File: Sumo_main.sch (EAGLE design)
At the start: 32 parts, among them U1 ATMEGA8U2AU, U2 SN65HVD3082, X1 MINI USB, X2 RS485, X4 IR Sensor 1, X5 IR Sensor 2, X6 IR Sensor 3, Y1 16MHz

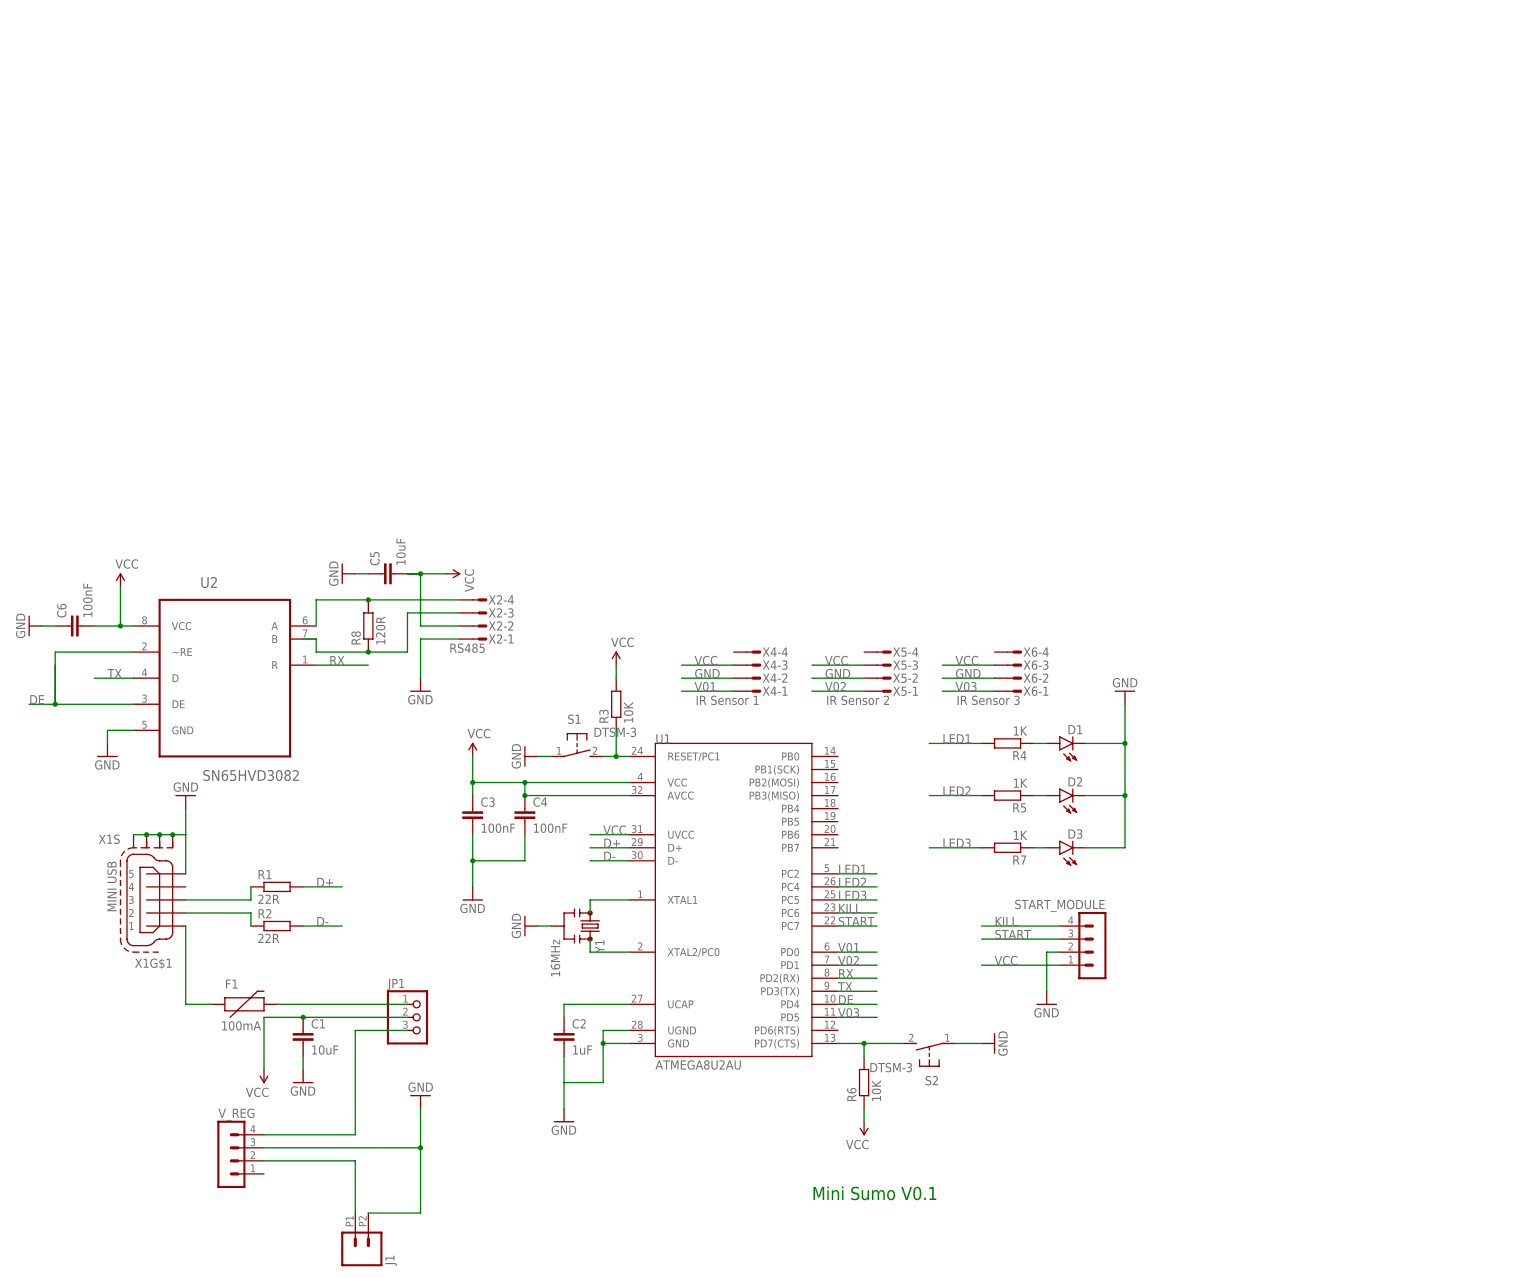
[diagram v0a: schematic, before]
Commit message: Version 2 - added comparator for sensor signals, redesigned board to be more compact.
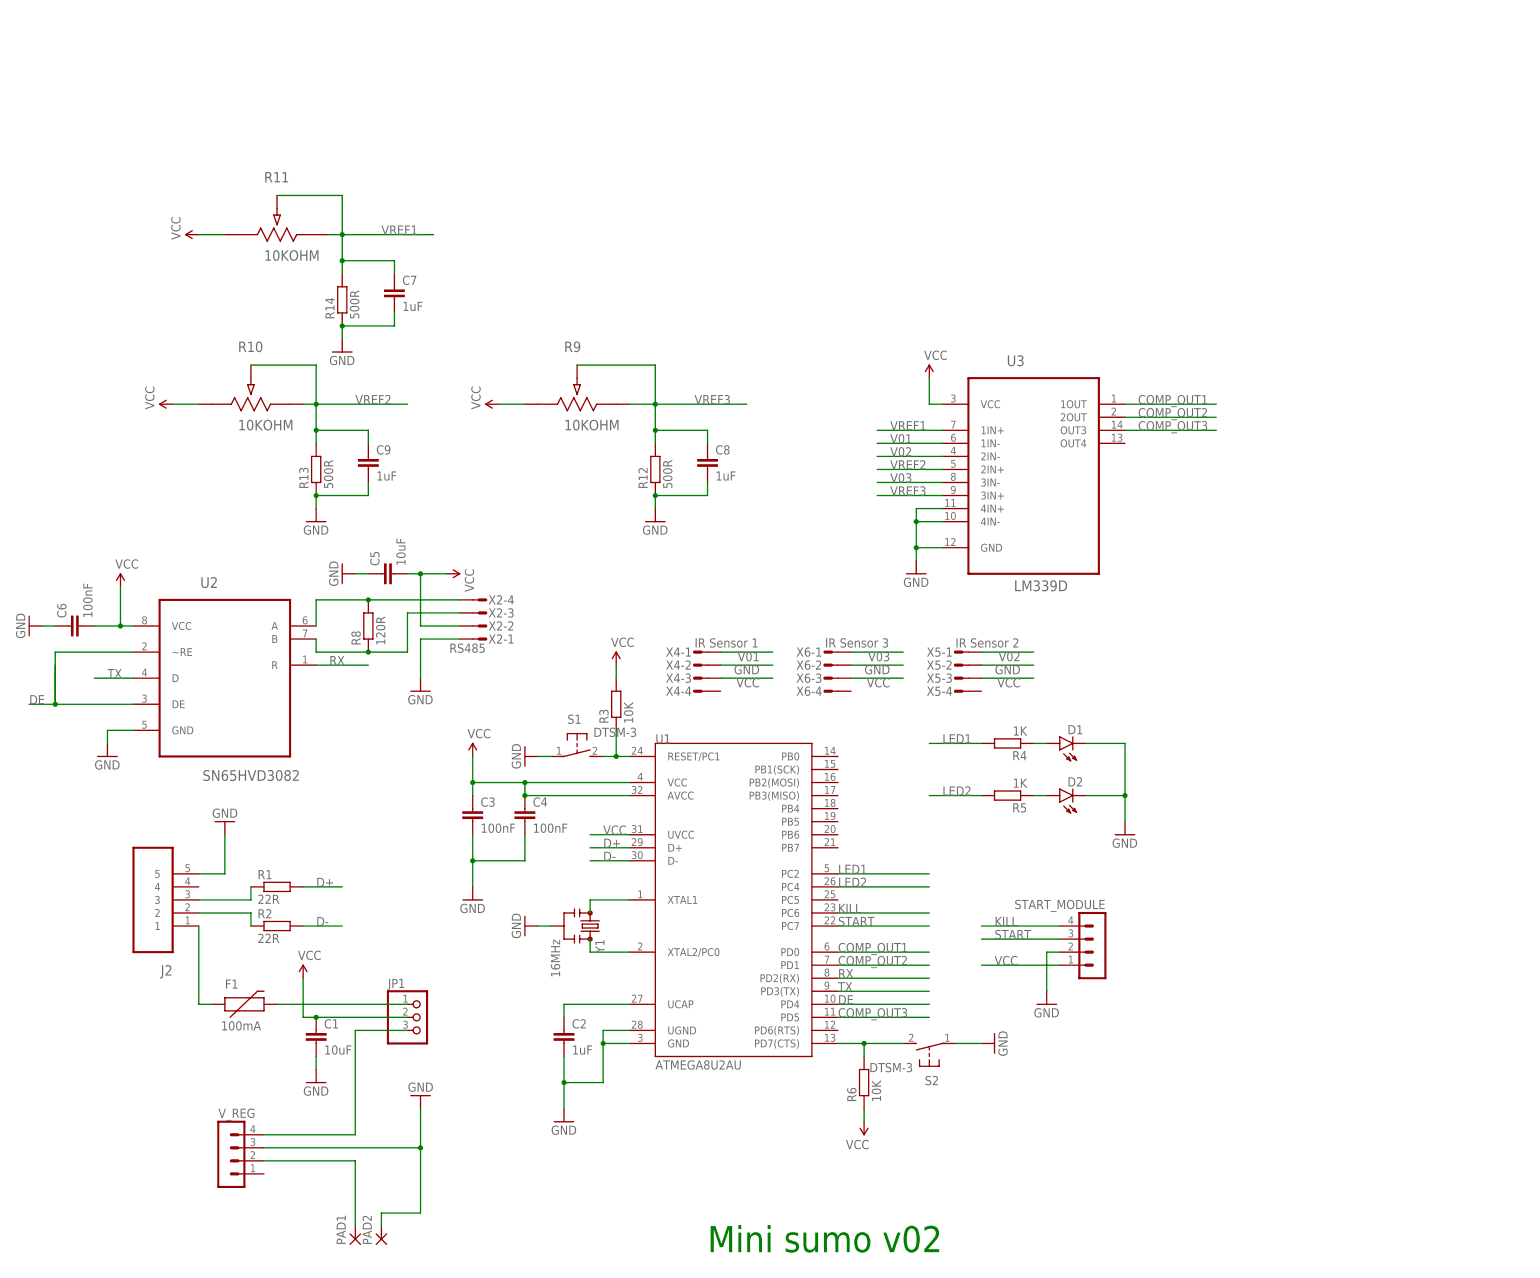
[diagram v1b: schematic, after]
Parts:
- removed D3: (no value), SparkFun-LED:LED0603
- removed J1: (no value), SparkFun-Connectors:M022.54MM_SCREWTERM
- removed R7: 1K, resistor:R-EU_R0603
- removed X1: MINI USB, con-cypressindustries:MINI-USB-SCHIELD-32005-201
- added C7, C8, C9: 1uF, SparkFun-Capacitors:CAP0603-CAP
- added J2: (no value), Molex-47346-0001:47346-0001
- added PAD1, PAD2: (no value), wirepad:2,15/1,0
- added R10, R11, R9: 10KOHM, Panasonic-Trimmer_Potentiometers:EVM3YSX50B14-3W
- added R12, R13, R14: 500R, resistor:R-EU_R0603
- added U3: LM339D, comparator:LM339D
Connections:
- removed net LED3: R7.2, U1.PC5
- removed net N$8: D3.A, R7.1
- new net COMP_OUT1: U1.PD0, U3.1OUT
- new net COMP_OUT2: U1.PD1, U3.2OUT
- new net COMP_OUT3: U1.PD5, U3.OUT3
- new net VREF1: C7.1, R11.2, R11.3, R14.2, U3.1IN+
- new net VREF2: C9.1, R10.2, R10.3, R13.2, U3.2IN+
- new net VREF3: C8.1, R12.2, R9.2, R9.3, U3.3IN+
- net GND: now also C7.2, C8.2, C9.2, J2.5, PAD2.P, R12.1, R13.1, R14.1, U3.4IN+, U3.4IN-, U3.GND; no longer D3.C, J1.2, X1G$1.5, X1S.S1, X1S.S2, X1S.S3, X1S.S4
- net N$1: now also J2.3; no longer X1G$1.3
- net N$2: now also J2.2; no longer X1G$1.2
- net N$23: now also PAD1.P; no longer J1.1
- net N$3: now also J2.1; no longer X1G$1.1
- net V01: now also U3.1IN-; no longer U1.PD0
- net V02: now also U3.2IN-; no longer U1.PD1
- net V03: now also U3.3IN-; no longer U1.PD5
- net VCC: now also R10.1, R11.1, R9.1, U3.VCC
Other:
- note added: "Mini sumo v02"
- note removed: "Mini Sumo V0.1"
- moved on the sheet: C1, X4-1, X4-2, X4-3, X4-4, X5-1, X5-2, X5-3, X5-4, X6-1, X6-2, X6-3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

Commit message: Added additional button for starting. Changed IR sensors' micromatches to pinheaders.
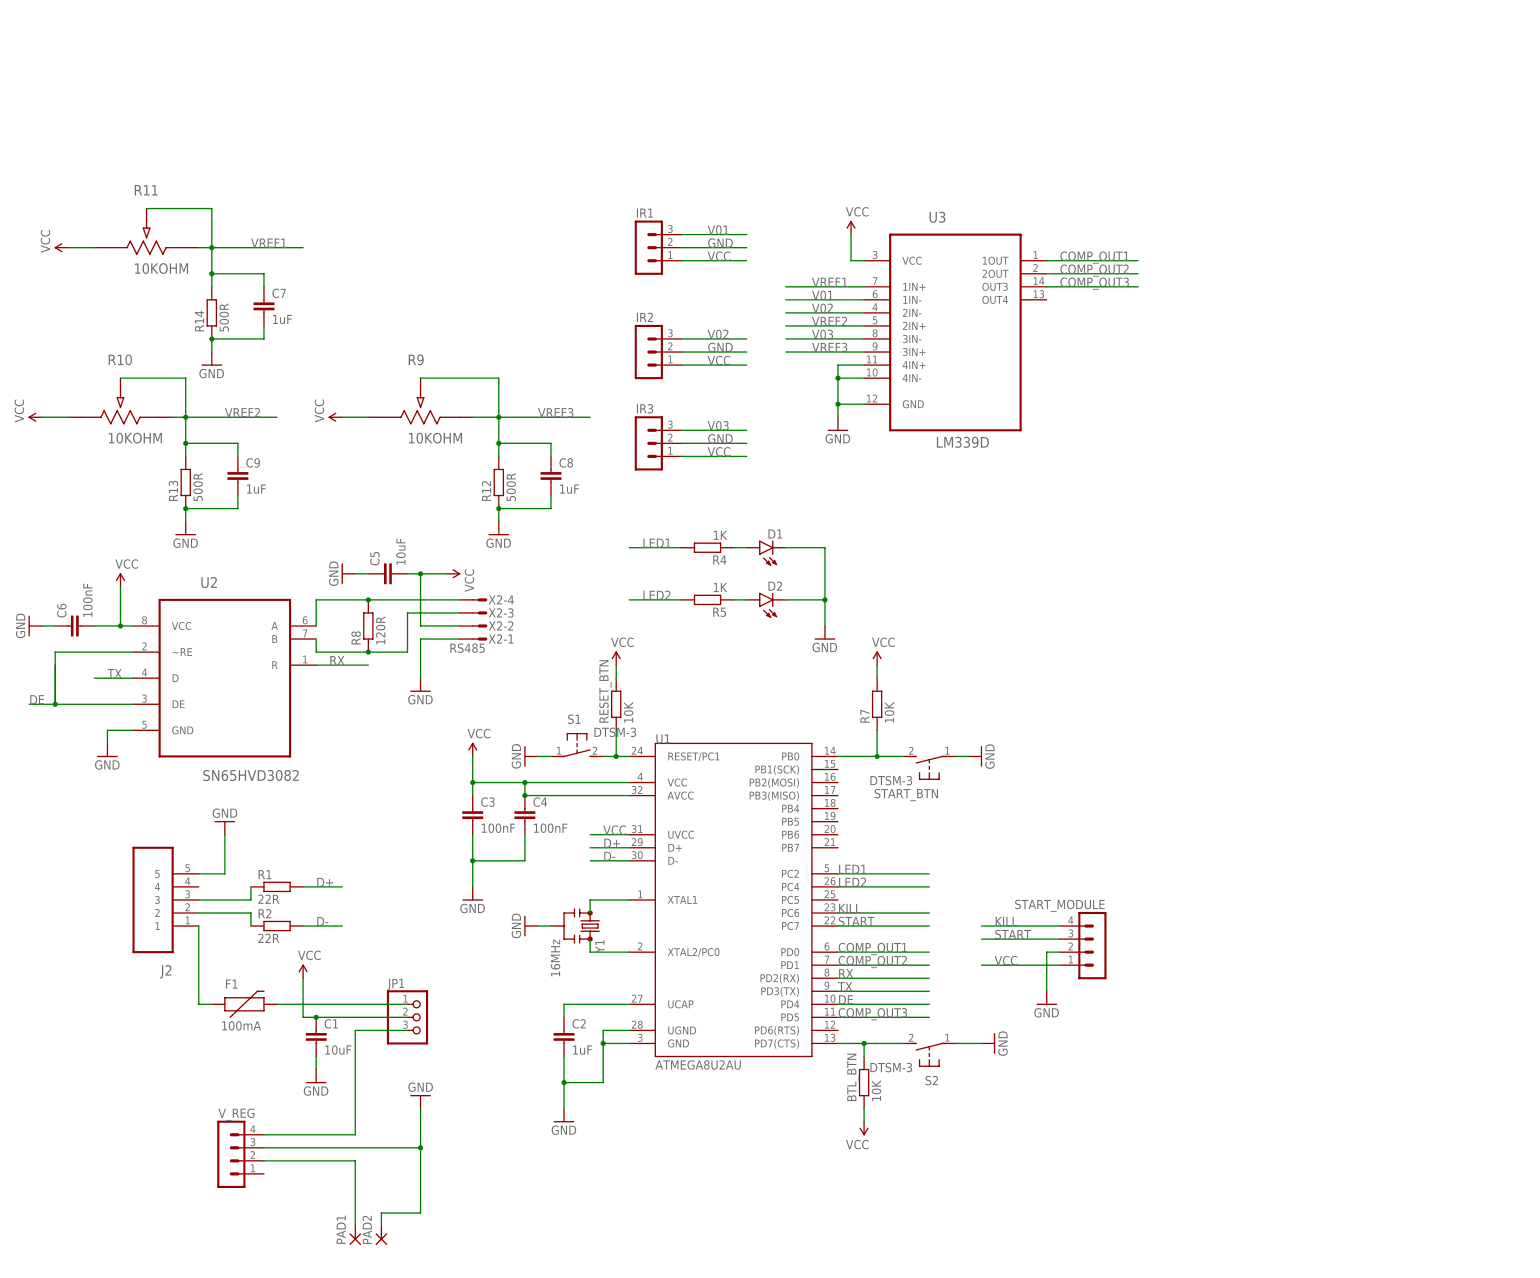
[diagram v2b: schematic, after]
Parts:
- removed X4: IR Sensor 1, con-amp-micromatch:MICROMATCH-4
- removed X5: IR Sensor 2, con-amp-micromatch:MICROMATCH-4
- removed X6: IR Sensor 3, con-amp-micromatch:MICROMATCH-4
- added IR1, IR2, IR3: (no value), con-lstb:MA03-1
- added R7: 10K, resistor:R-EU_R0603
- added START_BTN: DTSM-3, switch-tact:DTSM-3
- renumbered R3 to RESET_BTN, R6 to BTL_BTN
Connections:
- new net N$8: R7.1, START_BTN.2, U1.PB0
- net GND: now also IR1.2, IR3.2, START_BTN.1; no longer X4-2.S, X5-2.S, X6-2.S
- net V01: now also IR1.3; no longer X4-1.S
- net V02: now also IR2.3; no longer X5-1.S
- net V03: now also IR3.3; no longer X6-1.S
- net VCC: now also IR1.1, IR2.1, IR3.1, R7.2; no longer X4-3.S, X5-3.S, X6-3.S
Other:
- note removed: "Mini sumo v02"
- moved on the sheet: C7, C8, C9, D1, D2, R10, R11, R12, R13, R14, R4, R5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

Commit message: Add two IR reflection sensors to detect lines.
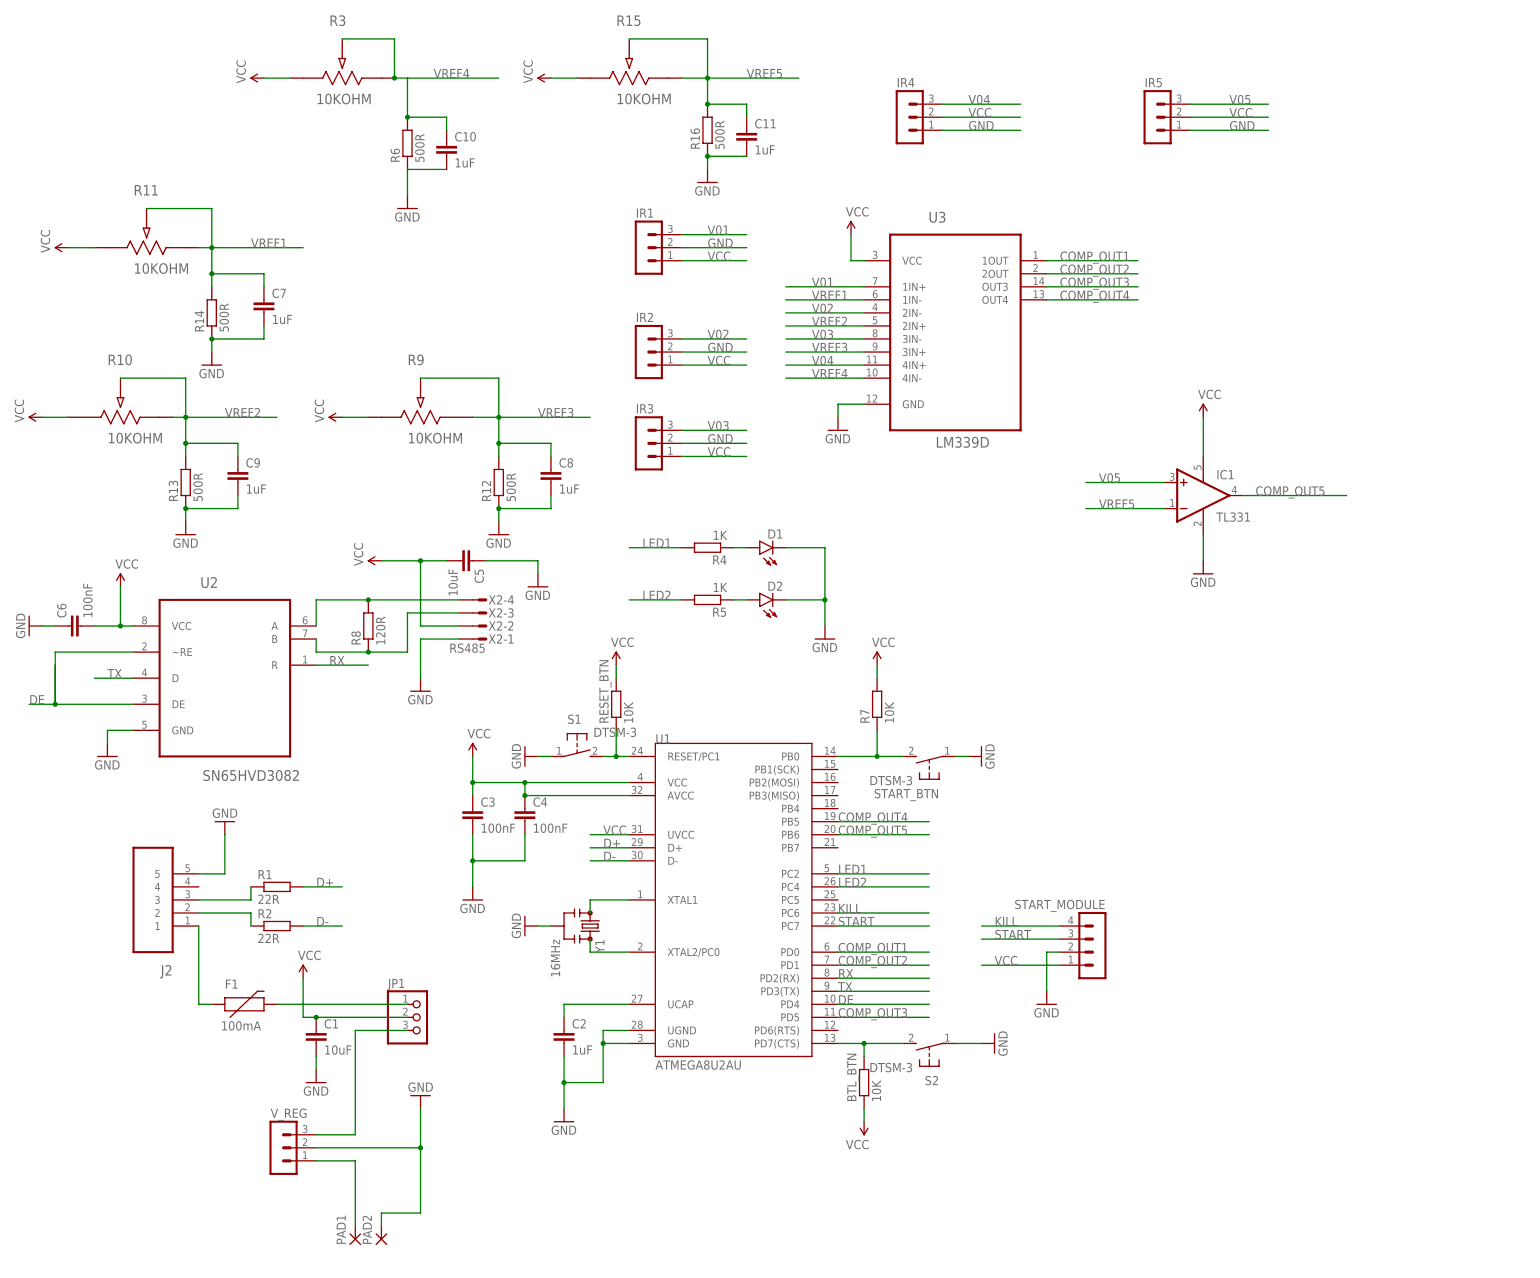
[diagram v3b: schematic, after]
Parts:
- added C10, C11: 1uF, SparkFun-Capacitors:CAP0603-CAP
- added IC1: TL331, linear:TL331
- added IR4, IR5: (no value), con-lstb:MA03-1
- added R15, R3: 10KOHM, Panasonic-Trimmer_Potentiometers:EVM3YSX50B14-3W
- added R16, R6: 500R, resistor:R-EU_R0603
- V_REG: device con-lstb:MA04-1 -> con-lstb:MA03-1
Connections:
- new net COMP_OUT4: U1.PB5, U3.OUT4
- new net COMP_OUT5: IC1.OUT, U1.PB6
- new net V04: IR4.3, U3.4IN+
- new net V05: IC1.+IN, IR5.3
- new net VREF4: C10.1, R3.2, R3.3, R6.2, U3.4IN-
- new net VREF5: C11.1, IC1.-IN, R15.2, R15.3, R16.2
- net GND: now also C10.2, C11.2, IC1.GND, IR4.1, IR5.1, R16.1, R6.1, V_REG.2; no longer U3.4IN+, U3.4IN-, V_REG.3
- net N$14: now also V_REG.3; no longer V_REG.4
- net N$23: now also V_REG.1; no longer V_REG.2
- net V01: now also U3.1IN+; no longer U3.1IN-
- net VCC: now also IC1.V+, IR4.2, IR5.2, R15.1, R3.1
- net VREF1: now also U3.1IN-; no longer U3.1IN+
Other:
- moved on the sheet: C5
